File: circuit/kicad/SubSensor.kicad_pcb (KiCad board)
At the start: 2 copper layers, 28 x 10 mm, 5 parts, among them J1 SH3, U1 S7136

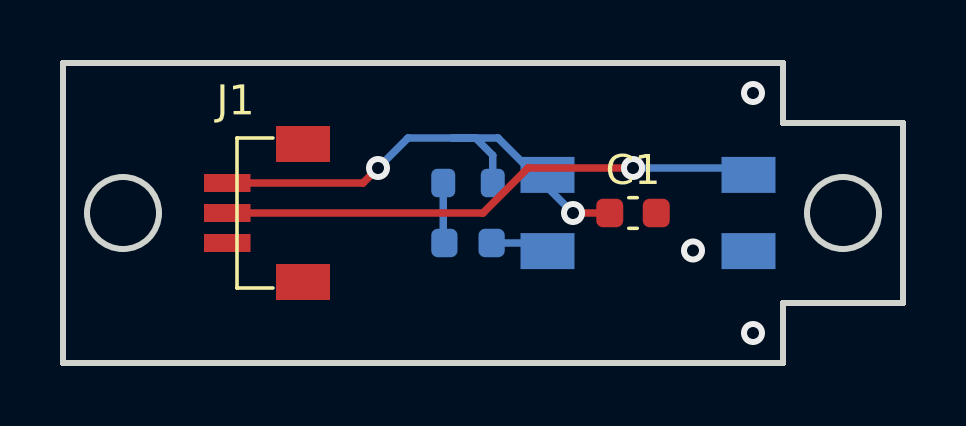
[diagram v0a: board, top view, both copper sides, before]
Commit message: フットプリントの問題は解消
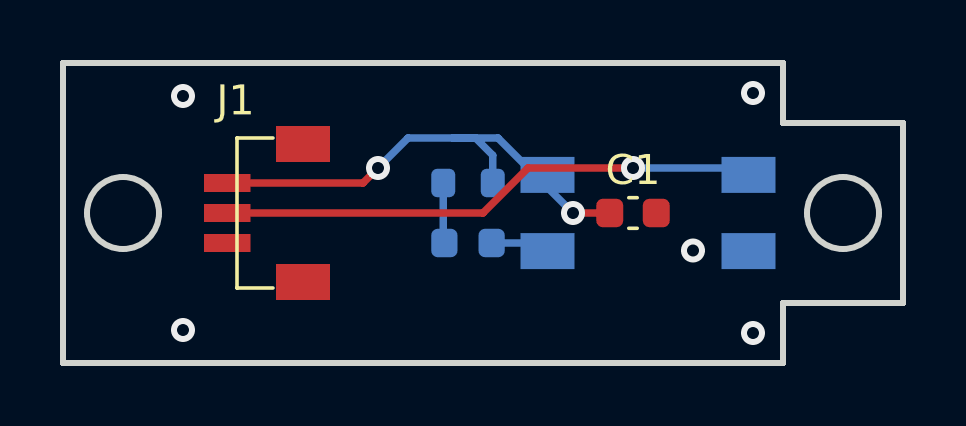
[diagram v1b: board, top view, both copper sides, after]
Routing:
- net GND: vias 3 -> 5
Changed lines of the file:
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@@
     (thickness 1.6)
     (drawings 14)
-    (tracks 26)
+    (tracks 28)
     (zones 0)
     (modules 5)
@@
   (via (at 23 1) (size 0.8) (drill 0.4) (layers F.Cu B.Cu) (net 2))
   (via (at 21 6.25) (size 0.8) (drill 0.4) (layers F.Cu B.Cu) (net 2))
+  (via (at 4 8.9) (size 0.8) (drill 0.4) (layers F.Cu B.Cu) (net 2))
+  (via (at 4 1.1) (size 0.8) (drill 0.4) (layers F.Cu B.Cu) (net 2))
   (segment (start 15.88 6) (end 16.15 6.27) (width 0.25) (layer B.Cu) (net 3) (status 30))
   (segment (start 14.2875 6) (end 15.88 6) (width 0.25) (layer B.Cu) (net 3) (status 30))

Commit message: 後はガーバデータ出してロゴ刺すだけ
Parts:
- R1: moved to F.Cu
- moved R1 2.33 mm to (11.4, 5.00), turned to 270 degrees
- moved D1 1.22 mm to (14.2, 5.00), turned to 90 degrees
- moved C1 0.50 mm to (19.5, 5.00), turned to 270 degrees
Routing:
- net +5V: track 17.3 -> 21.4 mm, vias 2 -> 1
- net Net-(D1-Pad2): track 2.02 -> 3.53 mm, vias 0 -> 1
- net Net-(D1-Pad1): track 1.97 -> 2.53 mm
- net GND: vias 5 -> 6

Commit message: export
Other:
- rule via_min_size: 0.4 -> 0.6
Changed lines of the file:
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@@
     (via_size 0.8)
     (via_drill 0.4)
-    (via_min_size 0.4)
+    (via_min_size 0.6)
     (via_min_drill 0.3)
     (user_via 0.6 0.3)
@@
       (effects (font (size 1 1) (thickness 0.15)))
     )
+    (fp_line (start -0.8 0.4) (end -0.8 -0.4) (layer F.Fab) (width 0.1))
+    (fp_line (start -0.8 -0.4) (end 0.8 -0.4) (layer F.Fab) (width 0.1))
+    (fp_line (start 0.8 -0.4) (end 0.8 0.4) (layer F.Fab) (width 0.1))
+    (fp_line (start 0.8 0.4) (end -0.8 0.4) (layer F.Fab) (width 0.1))
+    (fp_line (start -0.14058 -0.51) (end 0.14058 -0.51) (layer F.SilkS) (width 0.12))
+    (fp_line (start -0.14058 0.51) (end 0.14058 0.51) (layer F.SilkS) (width 0.12))
+    (fp_line (start -1.48 0.73) (end -1.48 -0.73) (layer F.CrtYd) (width 0.05))
+    (fp_line (start -1.48 -0.73) (end 1.48 -0.73) (layer F.CrtYd) (width 0.05))
+    (fp_line (start 1.48 -0.73) (end 1.48 0.73) (layer F.CrtYd) (width 0.05))
     (fp_line (start 1.48 0.73) (end -1.48 0.73) (layer F.CrtYd) (width 0.05))
-    (fp_line (start 1.48 -0.73) (end 1.48 0.73) (layer F.CrtYd) (width 0.05))
-    (fp_line (start -1.48 -0.73) (end 1.48 -0.73) (layer F.CrtYd) (width 0.05))
-    (fp_line (start -1.48 0.73) (end -1.48 -0.73) (layer F.CrtYd) (width 0.05))
-    (fp_line (start -0.14058 0.51) (end 0.14058 0.51) (layer F.SilkS) (width 0.12))
-    (fp_line (start -0.14058 -0.51) (end 0.14058 -0.51) (layer F.SilkS) (width 0.12))
-    (fp_line (start 0.8 0.4) (end -0.8 0.4) (layer F.Fab) (width 0.1))
-    (fp_line (start 0.8 -0.4) (end 0.8 0.4) (layer F.Fab) (width 0.1))
-    (fp_line (start -0.8 -0.4) (end 0.8 -0.4) (layer F.Fab) (width 0.1))
-    (fp_line (start -0.8 0.4) (end -0.8 -0.4) (layer F.Fab) (width 0.1))
     (fp_text user %R (at 0 0 90) (layer F.Fab)
       (effects (font (size 0.4 0.4) (thickness 0.06)))
@@
       (effects (font (size 1 1) (thickness 0.15)) (justify mirror))
     )
+    (fp_line (start 0.8 0.4) (end -0.5 0.4) (layer B.Fab) (width 0.1))
+    (fp_line (start -0.5 0.4) (end -0.8 0.1) (layer B.Fab) (width 0.1))
+    (fp_line (start -0.8 0.1) (end -0.8 -0.4) (layer B.Fab) (width 0.1))
+    (fp_line (start -0.8 -0.4) (end 0.8 -0.4) (layer B.Fab) (width 0.1))
+    (fp_line (start 0.8 -0.4) (end 0.8 0.4) (layer B.Fab) (width 0.1))
+    (fp_line (start 0.8 0.735) (end -1.485 0.735) (layer B.SilkS) (width 0.12))
+    (fp_line (start -1.485 0.735) (end -1.485 -0.735) (layer B.SilkS) (width 0.12))
+    (fp_line (start -1.485 -0.735) (end 0.8 -0.735) (layer B.SilkS) (width 0.12))
+    (fp_line (start -1.48 -0.73) (end -1.48 0.73) (layer B.CrtYd) (width 0.05))
+    (fp_line (start -1.48 0.73) (end 1.48 0.73) (layer B.CrtYd) (width 0.05))
+    (fp_line (start 1.48 0.73) (end 1.48 -0.73) (layer B.CrtYd) (width 0.05))
     (fp_line (start 1.48 -0.73) (end -1.48 -0.73) (layer B.CrtYd) (width 0.05))
-    (fp_line (start 1.48 0.73) (end 1.48 -0.73) (layer B.CrtYd) (width 0.05))
-    (fp_line (start -1.48 0.73) (end 1.48 0.73) (layer B.CrtYd) (width 0.05))
-    (fp_line (start -1.48 -0.73) (end -1.48 0.73) (layer B.CrtYd) (width 0.05))
-    (fp_line (start -1.485 -0.735) (end 0.8 -0.735) (layer B.SilkS) (width 0.12))
-    (fp_line (start -1.485 0.735) (end -1.485 -0.735) (layer B.SilkS) (width 0.12))
-    (fp_line (start 0.8 0.735) (end -1.485 0.735) (layer B.SilkS) (width 0.12))
-    (fp_line (start 0.8 -0.4) (end 0.8 0.4) (layer B.Fab) (width 0.1))
-    (fp_line (start -0.8 -0.4) (end 0.8 -0.4) (layer B.Fab) (width 0.1))
-    (fp_line (start -0.8 0.1) (end -0.8 -0.4) (layer B.Fab) (width 0.1))
-    (fp_line (start -0.5 0.4) (end -0.8 0.1) (layer B.Fab) (width 0.1))
-    (fp_line (start 0.8 0.4) (end -0.5 0.4) (layer B.Fab) (width 0.1))
     (fp_text user %R (at 0 0 90) (layer B.Fab)
       (effects (font (size 0.4 0.4) (thickness 0.06)) (justify mirror))
@@
       (effects (font (size 1 1) (thickness 0.15)))
     )
+    (fp_line (start 2.5 -2.2) (end 2.5 -1) (layer F.SilkS) (width 0.12))
+    (fp_line (start -2.5 -2.2) (end -2.5 -1) (layer F.SilkS) (width 0.12))
     (fp_line (start -2.5 -2.2) (end 2.5 -2.2) (layer F.SilkS) (width 0.12))
-    (fp_line (start -2.5 -2.2) (end -2.5 -1) (layer F.SilkS) (width 0.12))
-    (fp_line (start 2.5 -2.2) (end 2.5 -1) (layer F.SilkS) (width 0.12))
     (pad 3 smd rect (at 1 -2.525 90) (size 0.6 1.55) (layers F.Cu F.Paste F.Mask)
       (net 1 +5V))
@@
       (effects (font (size 1 1) (thickness 0.15)))
     )
+    (fp_line (start -0.8 0.4125) (end -0.8 -0.4125) (layer F.Fab) (width 0.1))
+    (fp_line (start -0.8 -0.4125) (end 0.8 -0.4125) (layer F.Fab) (width 0.1))
+    (fp_line (start 0.8 -0.4125) (end 0.8 0.4125) (layer F.Fab) (width 0.1))
+    (fp_line (start 0.8 0.4125) (end -0.8 0.4125) (layer F.Fab) (width 0.1))
+    (fp_line (start -0.237258 -0.5225) (end 0.237258 -0.5225) (layer F.SilkS) (width 0.12))
+    (fp_line (start -0.237258 0.5225) (end 0.237258 0.5225) (layer F.SilkS) (width 0.12))
+    (fp_line (start -1.48 0.73) (end -1.48 -0.73) (layer F.CrtYd) (width 0.05))
+    (fp_line (start -1.48 -0.73) (end 1.48 -0.73) (layer F.CrtYd) (width 0.05))
+    (fp_line (start 1.48 -0.73) (end 1.48 0.73) (layer F.CrtYd) (width 0.05))
     (fp_line (start 1.48 0.73) (end -1.48 0.73) (layer F.CrtYd) (width 0.05))
-    (fp_line (start 1.48 -0.73) (end 1.48 0.73) (layer F.CrtYd) (width 0.05))
-    (fp_line (start -1.48 -0.73) (end 1.48 -0.73) (layer F.CrtYd) (width 0.05))
-    (fp_line (start -1.48 0.73) (end -1.48 -0.73) (layer F.CrtYd) (width 0.05))
-    (fp_line (start -0.237258 0.5225) (end 0.237258 0.5225) (layer F.SilkS) (width 0.12))
-    (fp_line (start -0.237258 -0.5225) (end 0.237258 -0.5225) (layer F.SilkS) (width 0.12))
-    (fp_line (start 0.8 0.4125) (end -0.8 0.4125) (layer F.Fab) (width 0.1))
-    (fp_line (start 0.8 -0.4125) (end 0.8 0.4125) (layer F.Fab) (width 0.1))
-    (fp_line (start -0.8 -0.4125) (end 0.8 -0.4125) (layer F.Fab) (width 0.1))
-    (fp_line (start -0.8 0.4125) (end -0.8 -0.4125) (layer F.Fab) (width 0.1))
     (fp_text user %R (at 0 0 270) (layer F.Fab)
       (effects (font (size 0.4 0.4) (thickness 0.06)))
@@
       (effects (font (size 1 1) (thickness 0.15)) (justify mirror))
     )
+    (fp_line (start 2.4 2.9) (end 2.4 -2.9) (layer B.SilkS) (width 0.12))
+    (fp_line (start 2.4 -2.9) (end -2.4 -2.9) (layer B.SilkS) (width 0.12))
+    (fp_line (start -2.4 -2.9) (end -2.4 2.9) (layer B.SilkS) (width 0.12))
+    (fp_line (start -2.4 2.9) (end 2.4 2.9) (layer B.SilkS) (width 0.12))
     (fp_circle (center 0 1.450002) (end 0 0.966668) (layer B.SilkS) (width 0.12))
-    (fp_line (start -2.4 2.9) (end 2.4 2.9) (layer B.SilkS) (width 0.12))
-    (fp_line (start -2.4 -2.9) (end -2.4 2.9) (layer B.SilkS) (width 0.12))
-    (fp_line (start 2.4 -2.9) (end -2.4 -2.9) (layer B.SilkS) (width 0.12))
-    (fp_line (start 2.4 2.9) (end 2.4 -2.9) (layer B.SilkS) (width 0.12))
     (pad 1 smd rect (at -3.35 1.27) (size 1.8 1.2) (layers B.Cu B.Paste B.Mask)
       (net 3 "Net-(D1-Pad1)"))
